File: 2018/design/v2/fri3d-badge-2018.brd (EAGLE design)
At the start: 80.2 x 69.9 mm, 125 parts

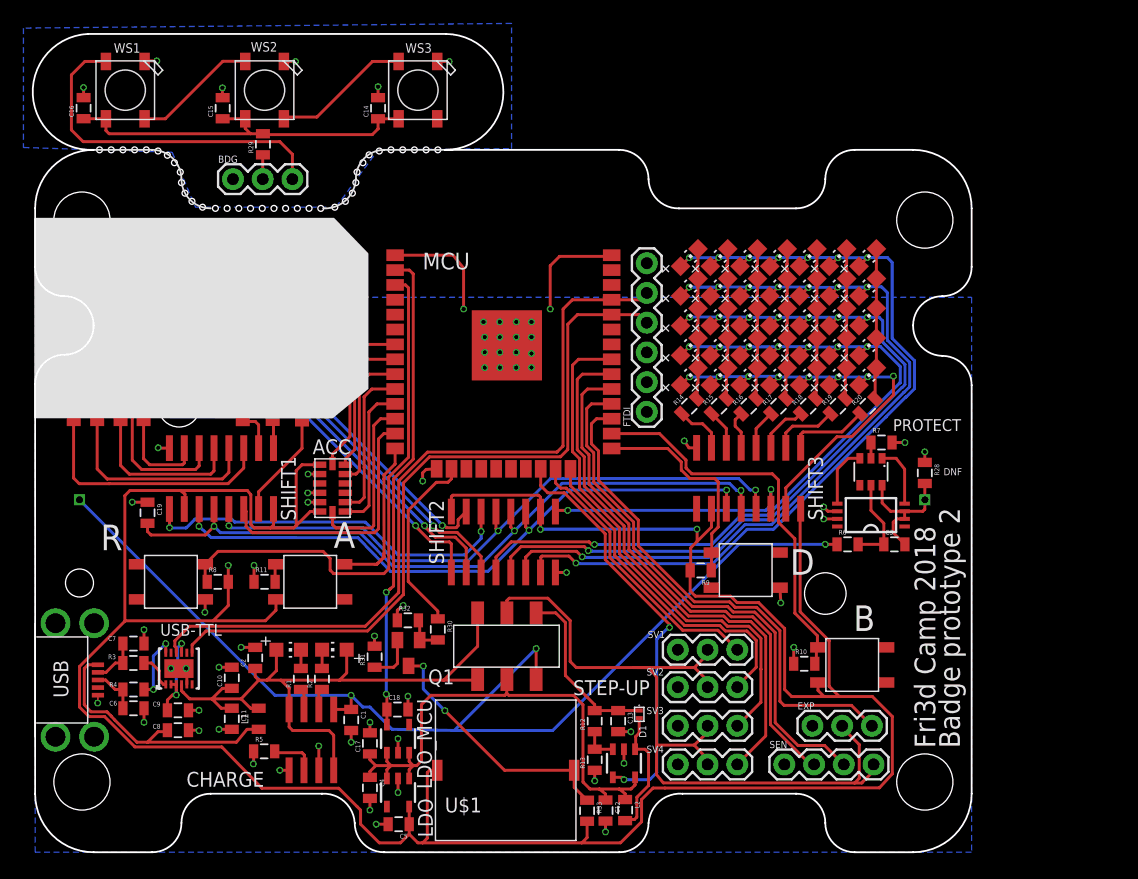
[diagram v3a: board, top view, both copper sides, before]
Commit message: changed step-up inductor + testpoints/shortcuts
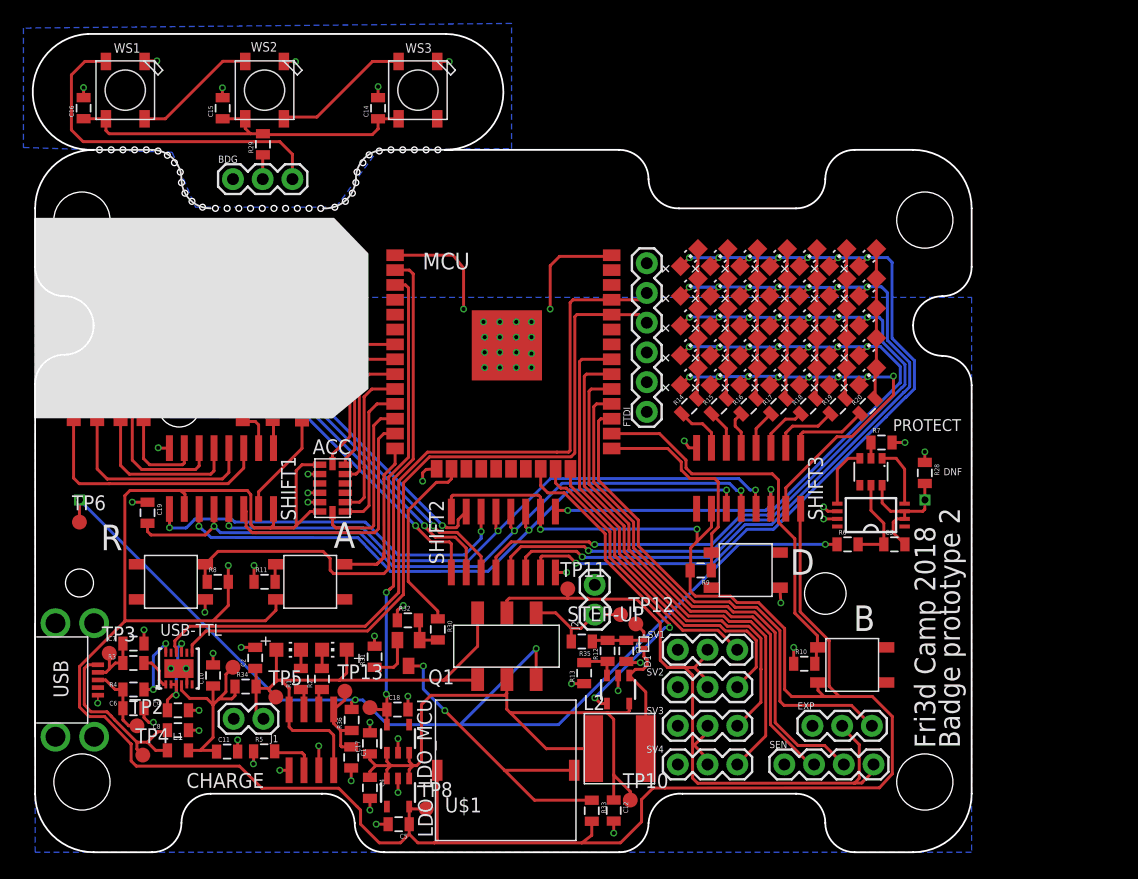
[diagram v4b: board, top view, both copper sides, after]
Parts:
- added J1, J2: (no value), SparkFun-Connectors:1X02
- added R34, R35, R36: 0, passive:0805
- added TP1, TP10, TP11, TP12, TP13, TP2, TP3, TP4, TP5, TP6, TP7, TP8, TP9: PTR1B1,27, testpad:B1,27
- L2: device passive:0805 -> passive:TYS6045
- moved R13 7.45 mm to (46.9, 15.3)
- moved L1 7.41 mm to (12.2, 8.70), turned to 0 degrees
- moved STEP-UP 6.32 mm to (49.8, 13.9)
- moved R12 6.10 mm to (48.9, 17.2)
- moved C13 6.04 mm to (50.5, 17.2)
- moved D1 6.01 mm to (52.0, 17.8)
- moved L2 5.27 mm to (49.9, 8.85), turned to 0 degrees
- moved C1 3.20 mm to (27.0, 8.10)
- moved C11 2.83 mm to (16.4, 8.60), turned to 0 degrees
- moved C10 1.61 mm to (15.2, 15.1)
- moved C12 0.70 mm to (49.4, 3.56)
- moved R33 0.40 mm to (47.5, 3.54)
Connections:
- new net N$1: C13.1, D1.P$2, R12.2, R35.1, TP12.TP
- new net N$22: C1.1, CHARGE.5, R36.1, TP13.TP
- new net USB-FILTERED: C10.1, C11.1, L1.2, R34.1, TP1.TP, USB-TTL.4
- net 3V3: now also TP8.TP
- net 3V3_MCU: now also TP9.TP
- net 5V: now also TP11.TP
- net D+: now also TP2.TP
- net D-: now also TP3.TP
- net GND: now also J1.2, J2.2
- net N$19: now also L2.P$2; no longer L2.2
- net USB-RAW: now also TP4.TP
- net VBAT: now also R36.2, TP6.TP; no longer C1.1, CHARGE.5
- net VCC: now also L2.P$1, TP10.TP; no longer L2.1
- net VSTEPUP: now also J2.1, R35.2, TP7.TP; no longer C13.1, D1.P$2, R12.2
- net VUSB: now also J1.1, R34.2, TP5.TP; no longer C10.1, C11.1, L1.2, USB-TTL.4
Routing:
- net USB-FILTERED: track 0.00 -> 18.3 mm
- net VCC: track 46.7 -> 56.8 mm
- net VUSB: track 58.0 -> 49.0 mm
- net N$22: track 0.00 -> 7.22 mm
- net 5V_ENABLE: track 36.1 -> 29.1 mm
- net USB-RAW: track 23.3 -> 16.6 mm
- net 5V: track 69.5 -> 62.9 mm
- net N$1: track 0.00 -> 6.13 mm
- net VSTEPUP: track 15.2 -> 9.36 mm
- net N$2: track 22.0 -> 27.5 mm
- net D+: track 4.07 -> 6.48 mm
- net 3V3: track 243.0 -> 244.8 mm
- net 3V3_MCU: track 41.2 -> 42.7 mm
- net D-: track 4.12 -> 5.58 mm
- net GND: track 70.3 -> 71.3 mm
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
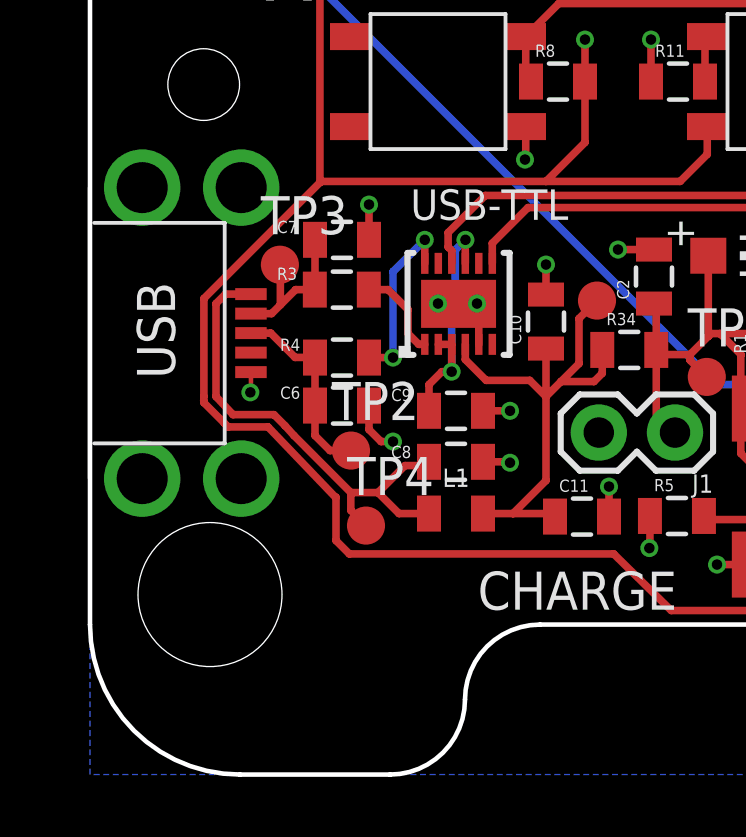
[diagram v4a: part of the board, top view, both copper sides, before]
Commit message: fixed USB GND/SHIELD issue
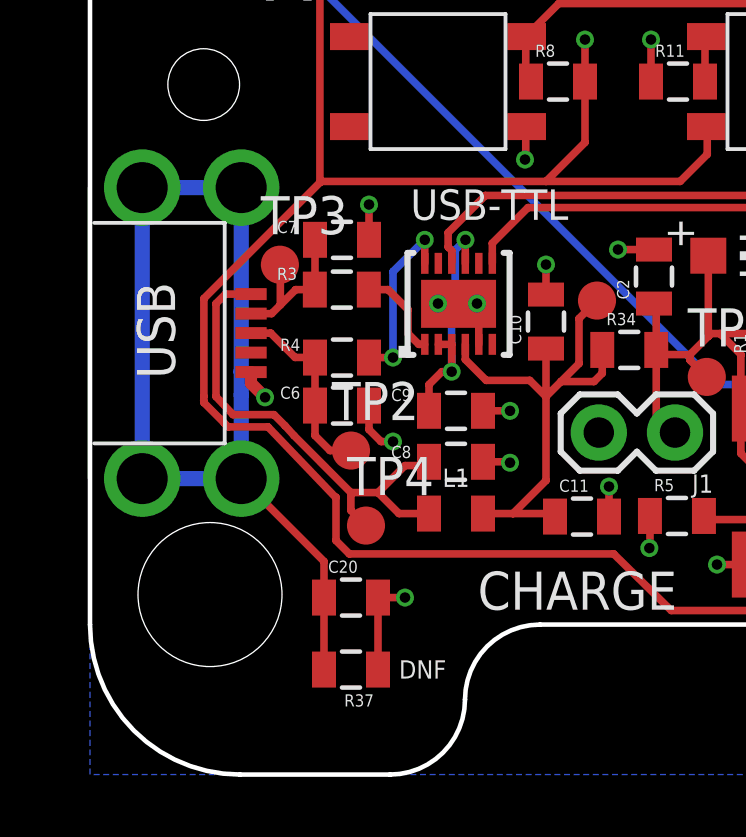
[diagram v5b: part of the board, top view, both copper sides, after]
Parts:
- added C20: 0.01uF, passive:0805
- added R37: 0, passive:0805
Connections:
- new net N$23: C20.1, R37.2, USB.6, USB.7, USB.8, USB.9
- net D+: now also USB.3; no longer USB.D+
- net D-: now also USB.2; no longer USB.D-
- net GND: now also C20.2, R37.1, USB.5; no longer USB.GND, USB.P$6, USB.P$7, USB.P$8, USB.P$9
- net USB-RAW: now also USB.1; no longer USB.VBUS
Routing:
- net N$23: track 0.00 -> 33.5 mm
- net GND: track 71.3 -> 74.9 mm, vias 60 -> 61
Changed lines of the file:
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@@
 <drawing>
 <settings>
-<setting alwaysvectorfont="yes"/>
+<setting alwaysvectorfont="no"/>
 <setting verticaltext="up"/>
 </settings>
@@
 <hole x="25.6" y="55.1" drill="0.5"/>
 <text x="77.6" y="32.2" size="0.6096" layer="25">DNF</text>
+<text x="10.3" y="3.2" size="0.6096" layer="25">DNF</text>
 </plain>
 <attributes>
@@
 <attribute name="TP_SIGNAL_NAME" value="" x="26.46" y="13.755" size="1.778" layer="27" display="off"/>
 </element>
+<element name="C20" library="passive" package="0805" value="0.01uF" x="8.7" y="5.9"/>
+<element name="R37" library="passive" package="0805" value="0" x="8.7" y="3.5" rot="R180"/>
 </elements>
 <signals>
 <signal name="GND">
-<contactref element="USB" pad="P$9"/>
-<contactref element="USB" pad="P$8"/>
-<contactref element="USB" pad="GND"/>
-<contactref element="USB" pad="P$7"/>
-<contactref element="USB" pad="P$6"/>
+<contactref element="USB" pad="5"/>
 <contactref element="USB-TTL" pad="5"/>
 <contactref element="USB-TTL" pad="13"/>
@@
 <wire x1="10.545" y1="34.52" x2="10.515" y2="34.55" width="0.254" layer="1"/>
 <via x="10.515" y="34.55" extent="1-16" drill="0.35"/>
-<via x="5.345" y="12.74" extent="1-16" drill="0.35"/>
-<wire x1="5.365" y1="13.415" x2="5.365" y2="12.76" width="0.1524" layer="1"/>
-<wire x1="5.365" y1="12.76" x2="5.345" y2="12.74" width="0.1524" layer="1"/>
 <wire x1="9.3" y1="17.825" x2="9.3" y2="19" width="0.254" layer="1"/>
 <via x="9.3" y="19" extent="1-16" drill="0.35"/>
@@
 <wire x1="50.6" y1="16.2" x2="51.7" y2="16.2" width="0.254" layer="1"/>
 <via x="51.7" y="16.2" extent="1-16" drill="0.35"/>
+<contactref element="C20" pad="2"/>
+<contactref element="R37" pad="1"/>
+<wire x1="5.365" y1="13.415" x2="5.365" y2="13.044" width="0.4064" layer="1"/>
+<wire x1="5.365" y1="13.044" x2="5.835" y2="12.574" width="0.4064" layer="1"/>
+<via x="5.835" y="12.574" extent="1-16" drill="0.35"/>
+<wire x1="9.6" y1="3.5" x2="9.6" y2="5.9" width="0.254" layer="1"/>
+<wire x1="9.6" y1="5.9" x2="10.5" y2="5.9" width="0.254" layer="1"/>
+<via x="10.5" y="5.9" extent="1-16" drill="0.35"/>
 </signal>
 <signal name="3V3">
@@
 </signal>
 <signal name="D+">
-<contactref element="USB" pad="D+"/>
+<contactref element="USB" pad="3"/>
 <contactref element="R4" pad="1"/>
 <contactref element="C6" pad="1"/>
@@
 </signal>
 <signal name="D-">
-<contactref element="USB" pad="D-"/>
+<contactref element="USB" pad="2"/>
 <contactref element="R3" pad="1"/>
 <contactref element="C7" pad="1"/>
@@
 </signal>
 <signal name="USB-RAW">
-<contactref element="USB" pad="VBUS"/>
+<contactref element="USB" pad="1"/>
 <contactref element="L1" pad="1"/>
 <contactref element="C8" pad="1"/>
@@
 <wire x1="26.45" y1="12.995" x2="26.46" y2="13.755" width="0.254" layer="1"/>
 </signal>
+<signal name="N$23">
+<contactref element="USB" pad="9"/>
+<contactref element="USB" pad="6"/>
+<contactref element="USB" pad="7"/>
+<contactref element="USB" pad="8"/>
+<contactref element="C20" pad="1"/>
+<contactref element="R37" pad="2"/>
+<wire x1="1.74" y1="19.565" x2="5.04" y2="19.565" width="0.508" layer="16"/>
+<wire x1="5.04" y1="19.565" x2="5.04" y2="13.4306125" width="0.508" layer="16"/>
+<wire x1="5.04" y1="13.4306125" x2="5.041" y2="13.4316125" width="0.508" layer="16"/>
+<wire x1="5.041" y1="13.4316125" x2="5.041" y2="12.6483875" width="0.508" layer="16"/>
+<wire x1="5.041" y1="12.6483875" x2="5.04" y2="12.0493875" width="0.508" layer="16"/>
+<wire x1="5.04" y1="12.0493875" x2="5.04" y2="9.865" width="0.508" layer="16"/>
+<wire x1="5.04" y1="9.865" x2="1.74" y2="9.865" width="0.508" layer="16"/>
+<wire x1="1.74" y1="9.865" x2="1.74" y2="19.565" width="0.508" layer="16"/>
+<wire x1="5.04" y1="9.865" x2="7.8" y2="7.105" width="0.254" layer="1"/>
+<wire x1="7.8" y1="7.105" x2="7.8" y2="5.9" width="0.254" layer="1"/>
+<wire x1="7.8" y1="5.9" x2="7.8" y2="3.5" width="0.254" layer="1"/>
+</signal>
 </signals>

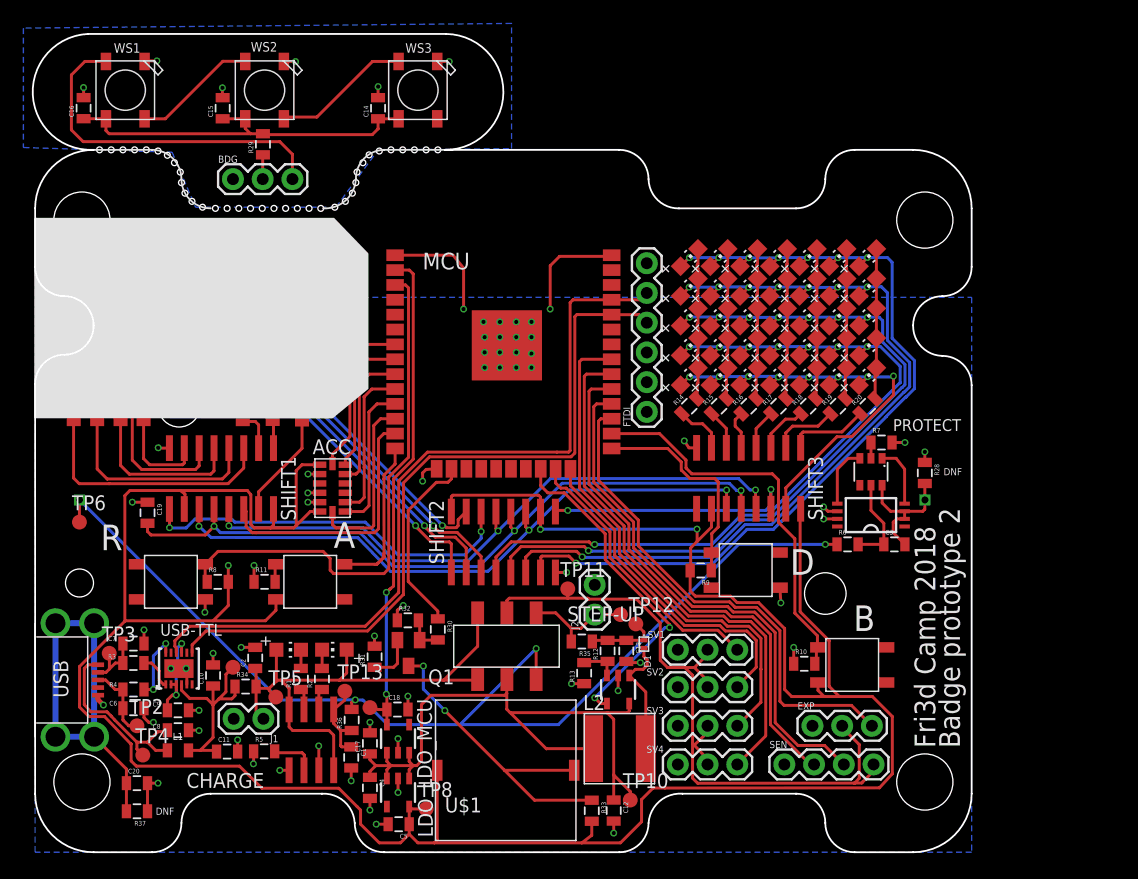
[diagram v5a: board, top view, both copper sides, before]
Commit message: added ESD protection, enlarged power planes/traces
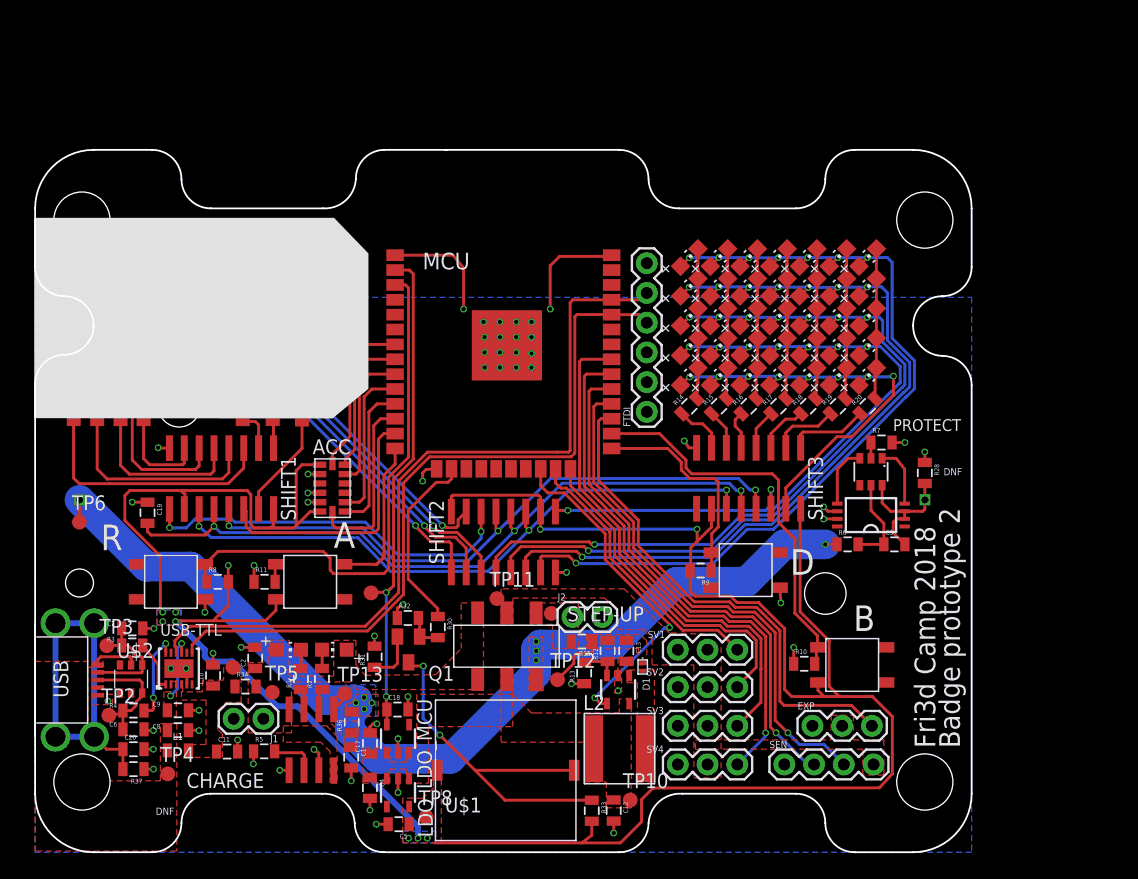
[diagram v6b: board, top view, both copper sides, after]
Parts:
- removed BDG: (no value), SparkFun-Connectors:1X03
- removed C14, C15, C16: 0.1uF, passive:0805
- removed R29: 0, passive:0805
- removed WS1, WS2, WS3: WS2812B5050, adafruit:WS2812B
- added U$2: IP4220CZ6, ic:SOT457R_PHILIPS
- moved TP9 9.80 mm to (28.7, 22.2)
- moved TP12 8.21 mm to (44.6, 14.7)
- moved TP11 6.11 mm to (39.5, 21.7)
- moved TP7 5.90 mm to (44.1, 20.4)
- moved R37 3.61 mm to (8.40, 7.10)
- moved C20 2.92 mm to (8.40, 8.80)
- moved TP4 2.67 mm to (11.3, 6.70)
- moved TP2 2.56 mm to (6.30, 11.7)
- moved D1 1.96 mm to (51.9, 15.8)
- moved J2 1.91 mm to (45.9, 20.1), turned to 0 degrees
- moved C6 1.80 mm to (8.40, 10.5)
- moved R4 1.80 mm to (8.40, 12.1)
- moved R3 1.50 mm to (8.29, 17.7)
- moved C7 1.30 mm to (8.30, 19.1)
- moved TP8 0.70 mm to (33.4, 3.00)
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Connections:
- removed net EXP_5V: C14.1, C15.1, C16.1, R29.2, WS1.1-VDD, WS2.1-VDD, WS3.1-VDD
- removed net EXP_GND: BDG.1, C14.2, C15.2, C16.2, WS1.3-GND, WS2.3-GND, WS3.3-GND
- removed net N$16: BDG.2, R29.1
- removed net N$17: WS1.2-DOUT, WS2.4-DIN
- removed net N$60: WS2.2-DOUT, WS3.4-DIN
- removed net N$61: BDG.3, WS1.4-DIN
- net D+: now also U$2.3
- net D-: now also U$2.4
- net USB-RAW: now also U$2.5
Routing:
- net 5V: track 62.9 -> 0.47 mm
- net VCC: track 56.8 -> 0.23 mm
- net VUSB: track 49.0 -> 0.56 mm
- net EXP_5V: track 32.5 -> 0.00 mm
- net 3V3: track 244.8 -> 214.1 mm, vias 3 -> 10
- net N$61: track 30.0 -> 0.00 mm
- net USB-FILTERED: track 18.3 -> 0.14 mm
- net USB-RAW: track 16.6 -> 4.20 mm
- net N$60: track 11.8 -> 0.00 mm
- net N$17: track 10.6 -> 0.00 mm
- net N$19: track 10.3 -> 0.00 mm
- net VSTEPUP: track 9.36 -> 0.00 mm
- net VBAT: track 93.8 -> 87.0 mm, vias 3 -> 8
- net GND: track 74.9 -> 68.8 mm
- net EXP_GND: track 5.76 -> 0.00 mm, vias 6 -> 0
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- added copper zone on layer 1, net 3V3
- added copper zone on layer 16, net 3V3
- added copper zone on layer 1, net 5V
- added copper zone on layer 1, net GND
- added copper zone on layer 1, net N$1
- added copper zone on layer 1, net N$19
- added copper zone on layer 1, net N$22
- added copper zone on layer 1, net N$6
- added copper zone on layer 1, net USB-FILTERED
- added copper zone on layer 1, net USB-RAW
- added copper zone on layer 1, net VBAT
- added copper zone on layer 16, net VBAT
- added copper zone on layer 1, net VCC
- added copper zone on layer 1, net VSTEPUP
- added copper zone on layer 1, net VUSB
- removed copper zone on layer 16, net EXP_GND
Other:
- board size 80.2 x 69.9 mm -> 80 x 60 mm

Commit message: added polygons for GND near DW-01 + cut corners
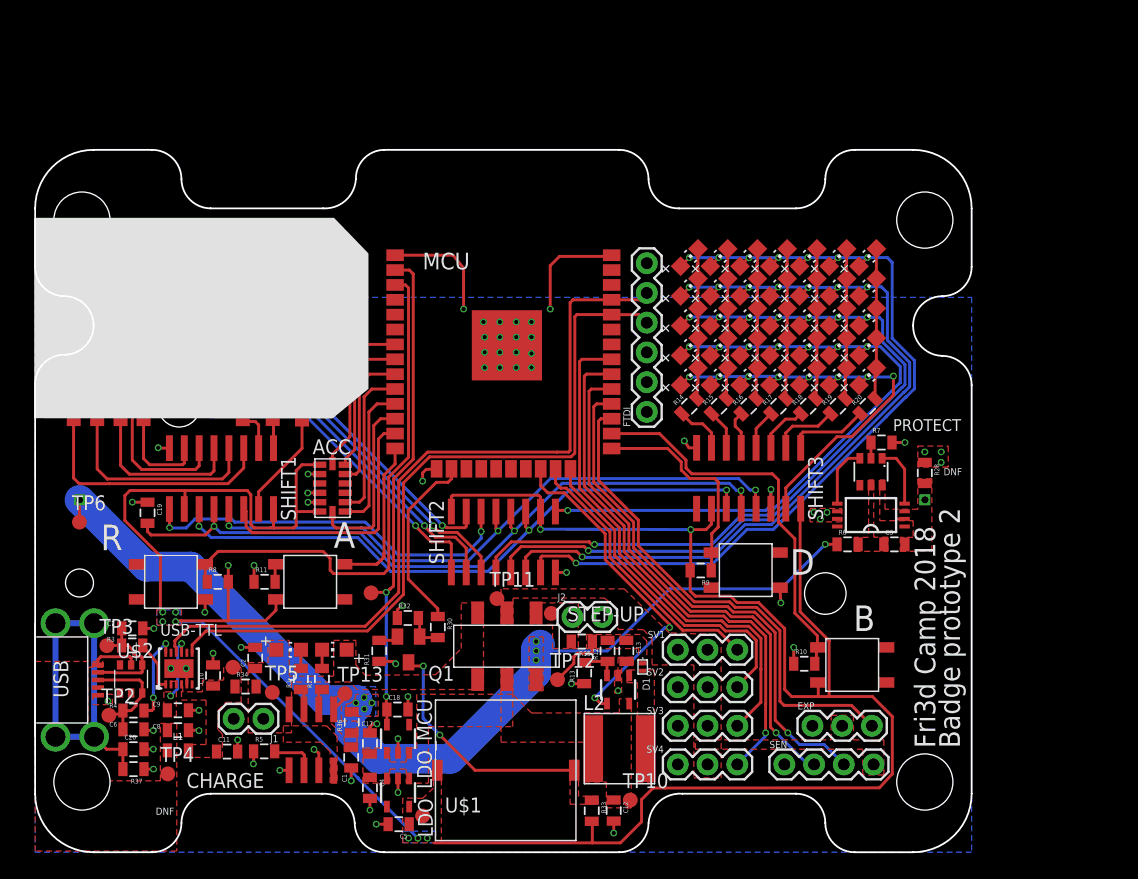
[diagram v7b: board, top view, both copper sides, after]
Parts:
- moved R31 0.64 mm to (29.4, 17.2), turned to 270 degrees
- moved TP8 0.32 mm to (33.1, 3.10)
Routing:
- net N$2: track 31.8 -> 20.8 mm
- net N$62: track 11.8 -> 0.89 mm
- net N$13: track 7.71 -> 0.00 mm
- net 3V3: track 214.1 -> 210.1 mm
- net GND: track 68.8 -> 65.7 mm, vias 61 -> 64
- net N$63: track 4.38 -> 1.68 mm
- net VBAT: track 87.0 -> 87.6 mm
- added copper zone on layer 1, net N$13
- added copper zone on layer 1, net N$2
- added copper zone on layer 1, net N$62
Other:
- outline, holes or cut-outs redrawn
